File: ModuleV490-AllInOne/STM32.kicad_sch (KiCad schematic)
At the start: 45 parts, among them J10 RELAY, J11 TEMP1, J12 TEMP2, J13 TEMP3, J2 BOOT_MODE, J3 UART_PROG, J4 ST_LINK, J8 TXRX, Q1 AO3401A, U13 EL3H7(B)(TA)-G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

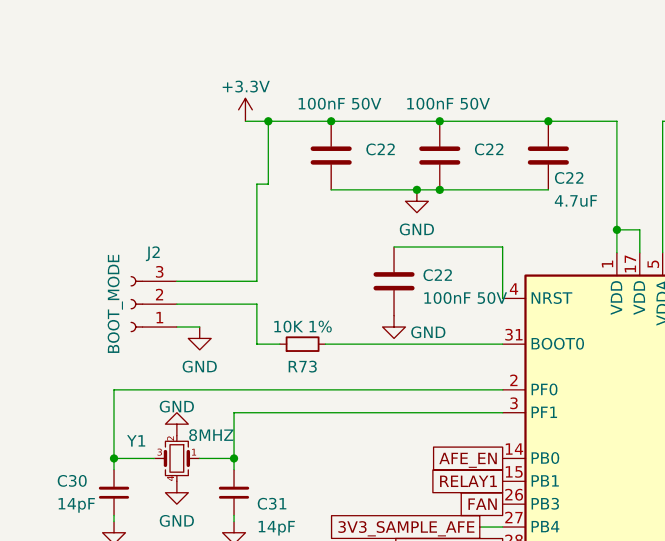
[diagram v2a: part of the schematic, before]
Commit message: Added SMT switch to replace jumper pins
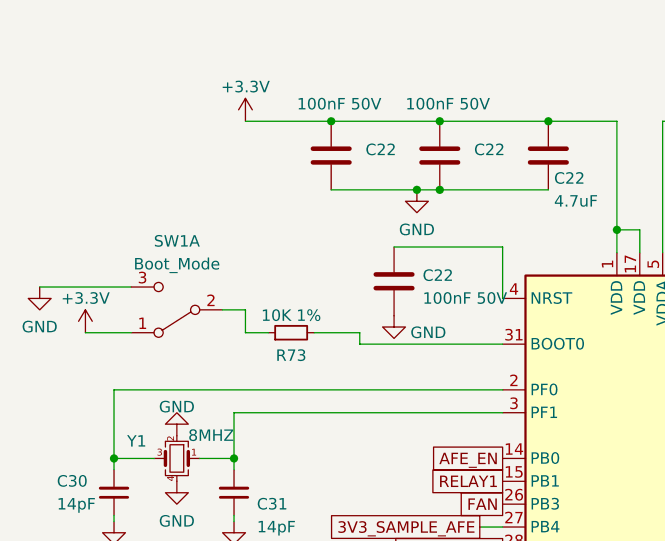
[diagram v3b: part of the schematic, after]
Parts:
- removed J2: BOOT_MODE, Connector_PinHeader_2.54mm:PinHeader_1x03_P2.54mm_Vertical, symbol Connector:Conn_01x03_Socket
- added SW1: Boot_Mode, SHOU_HAN:MST22D18G2 125, symbol Switch:SW_DPDT_x2
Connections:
- net +3.3V: now also SW1.1 (A)
- net GND: now also SW1.3 (C)
- net at R73.1: now also SW1.2 (B)
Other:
- moved on the sheet: R73
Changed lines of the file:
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@@
   (junction (at 214.63 138.43) (diameter 0) (color 0 0 0 0)
-  )
-  (junction (at 43.18 45.085) (diameter 0) (color 0 0 0 0)
   )
   (junction (at 39.37 82.55) (diameter 0) (color 0 0 0 0)
@@
   (no_connect (at 97.155 72.39))
   (no_connect (at 97.155 69.85))
+  (wire (pts (xy 53.34 68.58) (xy 53.34 69.85))
+    (stroke (width 0) (type default))
+  )
   (wire (pts (xy 93.345 52.705) (xy 95.885 52.705))
     (stroke (width 0) (type default))
@@
     (stroke (width 0) (type default))
   )
-  (wire (pts (xy 41.91 69.85) (xy 44.45 69.85))
+  (wire (pts (xy 40.64 68.58) (xy 43.18 68.58))
     (stroke (width 0) (type default))
   )
@@
     (stroke (width 0) (type default))
   )
-  (wire (pts (xy 49.53 69.85) (xy 69.215 69.85))
+  (wire (pts (xy 48.26 68.58) (xy 53.34 68.58))
     (stroke (width 0) (type default))
   )
@@
     (stroke (width 0) (type default))
   )
-  (wire (pts (xy 41.91 65.405) (xy 33.02 65.405))
-    (stroke (width 0) (type default))
-  )
   (wire (pts (xy 103.505 67.31) (xy 97.155 67.31))
     (stroke (width 0) (type default))
@@
     (stroke (width 0) (type default))
   )
+  (wire (pts (xy 40.64 68.58) (xy 40.64 66.04))
+    (stroke (width 0) (type default))
+  )
   (wire (pts (xy 97.155 92.71) (xy 139.065 92.71))
     (stroke (width 0) (type default))
@@
     (stroke (width 0) (type default))
   )
+  (wire (pts (xy 17.78 63.5) (xy 27.94 63.5))
+    (stroke (width 0) (type default))
+  )
   (wire (pts (xy 228.6 83.185) (xy 228.6 77.47))
     (stroke (width 0) (type default))
@@
     (stroke (width 0) (type default))
   )
-  (wire (pts (xy 41.91 69.85) (xy 41.91 65.405))
-    (stroke (width 0) (type default))
-  )
   (wire (pts (xy 55.88 176.53) (xy 55.88 177.8))
     (stroke (width 0) (type default))
@@
     (stroke (width 0) (type default))
   )
-  (wire (pts (xy 40.64 45.085) (xy 43.18 45.085))
-    (stroke (width 0) (type default))
-  )
-  (wire (pts (xy 33.02 67.945) (xy 35.56 67.945))
+  (wire (pts (xy 40.64 45.085) (xy 50.165 45.085))
     (stroke (width 0) (type default))
   )
@@
     (stroke (width 0) (type default))
   )
-  (wire (pts (xy 41.91 52.07) (xy 43.18 52.07))
-    (stroke (width 0) (type default))
-  )
   (wire (pts (xy 227.965 88.265) (xy 234.95 88.265))
     (stroke (width 0) (type default))
@@
     (stroke (width 0) (type default))
   )
-  (wire (pts (xy 43.18 52.07) (xy 43.18 45.085))
-    (stroke (width 0) (type default))
-  )
   (wire (pts (xy 84.455 59.69) (xy 84.455 57.15))
     (stroke (width 0) (type default))
@@
     (stroke (width 0) (type default))
   )
+  (wire (pts (xy 53.34 69.85) (xy 69.215 69.85))
+    (stroke (width 0) (type default))
+  )
   (wire (pts (xy 41.91 151.13) (xy 41.91 152.4))
     (stroke (width 0) (type default))
@@
     (stroke (width 0) (type default))
   )
+  (wire (pts (xy 22.86 68.58) (xy 27.94 68.58))
+    (stroke (width 0) (type default))
+  )
   (wire (pts (xy 26.035 88.9) (xy 26.035 89.535))
     (stroke (width 0) (type default))
   )
-  (wire (pts (xy 33.02 62.865) (xy 41.91 62.865))
-    (stroke (width 0) (type default))
-  )
   (wire (pts (xy 227.33 84.455) (xy 234.95 84.455))
     (stroke (width 0) (type default))
@@
     (stroke (width 0) (type default))
   )
-  (wire (pts (xy 43.18 45.085) (xy 50.165 45.085))
-    (stroke (width 0) (type default))
-  )
   (wire (pts (xy 194.31 137.795) (xy 194.31 134.62))
     (stroke (width 0) (type default))
   )
+  (wire (pts (xy 40.64 66.04) (xy 38.1 66.04))
+    (stroke (width 0) (type default))
+  )
   (wire (pts (xy 214.63 150.495) (xy 214.63 151.13))
     (stroke (width 0) (type default))
@@
   )
   (wire (pts (xy 103.505 64.77) (xy 97.155 64.77))
-    (stroke (width 0) (type default))
-  )
-  (wire (pts (xy 41.91 62.865) (xy 41.91 52.07))
     (stroke (width 0) (type default))
   )
@@
     )
   )
+  (symbol (lib_id "power:+3.3V") (at 22.86 68.58 0) (unit 1)
+    (in_bom yes) (on_board yes) (dnp no) (fields_autoplaced)
+    (property "Reference" "#PWR024" (at 22.86 72.39 0)
+      (effects (font (size 1.27 1.27)) hide)
+    )
+    (property "Value" "+3.3V" (at 22.86 64.77 0)
+      (effects (font (size 1.27 1.27)))
+    )
+    (property "Footprint" "" (at 22.86 68.58 0)
+      (effects (font (size 1.27 1.27)) hide)
+    )
+    (property "Datasheet" "" (at 22.86 68.58 0)
+      (effects (font (size 1.27 1.27)) hide)
+    )
+    (pin "1")
+    (instances
+      (project "Module_16S"
+        (path "/e63e39d7-6ac0-4ffd-8aa3-1841a4541b55"
+          (reference "#PWR024") (unit 1)
+        )
+        (path "/e63e39d7-6ac0-4ffd-8aa3-1841a4541b55/f65e9c34-bb90-4d0c-b988-67c6b9ba4d90"
+          (reference "#PWR08") (unit 1)
+        )
+      )
+    )
+  )
   (symbol (lib_id "Relay_SolidState:ASSR-1218") (at 45.72 179.07 0) (unit 1)
     (in_bom yes) (on_board yes) (dnp no) (fields_autoplaced)
@@
         (path "/e63e39d7-6ac0-4ffd-8aa3-1841a4541b55/f65e9c34-bb90-4d0c-b988-67c6b9ba4d90"
           (reference "TH3") (unit 1)
+        )
+      )
+    )
+  )
+  (symbol (lib_id "Switch:SW_DPDT_x2") (at 33.02 66.04 180) (unit 1)
+    (in_bom yes) (on_board yes) (dnp no) (fields_autoplaced)
+    (property "Reference" "SW1" (at 33.02 58.42 0)
+      (effects (font (size 1.27 1.27)))
+    )
+    (property "Value" "Boot_Mode" (at 33.02 60.96 0)
+      (effects (font (size 1.27 1.27)))
+    )
+    (property "Footprint" "SHOU_HAN:MST22D18G2 125" (at 33.02 66.04 0)
+      (effects (font (size 1.27 1.27)) hide)
+    )
+    (property "Datasheet" "~" (at 33.02 66.04 0)
+      (effects (font (size 1.27 1.27)) hide)
+    )
+    (property "LCSCStockCode" "C2906280" (at 33.02 66.04 0)
+      (effects (font (size 1.27 1.27)) hide)
+    )
+    (pin "1")
+    (pin "2")
+    (pin "3")
+    (pin "4")
+    (pin "5")
+    (pin "6")
+    (instances
+      (project "Module_16S"
+        (path "/e63e39d7-6ac0-4ffd-8aa3-1841a4541b55/f65e9c34-bb90-4d0c-b988-67c6b9ba4d90"
+          (reference "SW1") (unit 1)
         )
       )
@@
     )
   )
-  (symbol (lib_id "power:GND") (at 35.56 67.945 0) (unit 1)
-    (in_bom yes) (on_board yes) (dnp no) (fields_autoplaced)
-    (property "Reference" "#PWR036" (at 35.56 74.295 0)
-      (effects (font (size 1.27 1.27)) hide)
-    )
-    (property "Value" "GND" (at 35.56 72.39 0)
-      (effects (font (size 1.27 1.27)))
-    )
-    (property "Footprint" "" (at 35.56 67.945 0)
-      (effects (font (size 1.27 1.27)) hide)
-    )
-    (property "Datasheet" "" (at 35.56 67.945 0)
+  (symbol (lib_id "power:GND") (at 17.78 63.5 0) (unit 1)
+    (in_bom yes) (on_board yes) (dnp no) (fields_autoplaced)
+    (property "Reference" "#PWR036" (at 17.78 69.85 0)
+      (effects (font (size 1.27 1.27)) hide)
+    )
+    (property "Value" "GND" (at 17.78 67.945 0)
+      (effects (font (size 1.27 1.27)))
+    )
+    (property "Footprint" "" (at 17.78 63.5 0)
+      (effects (font (size 1.27 1.27)) hide)
+    )
+    (property "Datasheet" "" (at 17.78 63.5 0)
       (effects (font (size 1.27 1.27)) hide)
     )
@@
         (path "/e63e39d7-6ac0-4ffd-8aa3-1841a4541b55/f65e9c34-bb90-4d0c-b988-67c6b9ba4d90"
           (reference "D19") (unit 1)
-        )
-      )
-    )
-  )
-  (symbol (lib_id "Connector:Conn_01x03_Socket") (at 27.94 65.405 180) (unit 1)
-    (in_bom yes) (on_board yes) (dnp no)
-    (property "Reference" "J2" (at 30.48 59.69 0)
-      (effects (font (size 1.27 1.27)))
-    )
-    (property "Value" "BOOT_MODE" (at 26.035 65.405 90)
-      (effects (font (size 1.27 1.27)))
-    )
-    (property "Footprint" "Connector_PinHeader_2.54mm:PinHeader_1x03_P2.54mm_Vertical" (at 27.94 65.405 0)
-      (effects (font (size 1.27 1.27)) hide)
-    )
-    (property "Datasheet" "~" (at 27.94 65.405 0)
-      (effects (font (size 1.27 1.27)) hide)
-    )
-    (property "PartNumber" "DZ254R-11-03-63" (at 27.94 65.405 0)
-      (effects (font (size 1.27 1.27)) hide)
-    )
-    (property "LCSCStockCode" "C2935909" (at 27.94 65.405 0)
-      (effects (font (size 1.27 1.27)) hide)
-    )
-    (pin "1")
-    (pin "2")
-    (pin "3")
-    (instances
-      (project "Module_16S"
-        (path "/e63e39d7-6ac0-4ffd-8aa3-1841a4541b55/f65e9c34-bb90-4d0c-b988-67c6b9ba4d90"
-          (reference "J2") (unit 1)
         )
       )
@@
     )
   )
-  (symbol (lib_id "Device:R_Small") (at 46.99 69.85 90) (unit 1)
+  (symbol (lib_id "Device:R_Small") (at 45.72 68.58 90) (unit 1)
     (in_bom yes) (on_board yes) (dnp no)
-    (property "Reference" "R73" (at 46.99 72.39 90)
-      (effects (font (size 1.27 1.27)))
-    )
-    (property "Value" "10K 1%" (at 46.99 67.945 90)
-      (effects (font (size 1.27 1.27)))
-    )
-    (property "Footprint" "Resistor_SMD:R_0603_1608Metric" (at 46.99 69.85 0)
-      (effects (font (size 1.27 1.27)) hide)
-    )
-    (property "Datasheet" "~" (at 46.99 69.85 0)
-      (effects (font (size 1.27 1.27)) hide)
-    )
-    (property "PartNumber" "0603WAF1002T5E" (at 46.99 69.85 0)
-      (effects (font (size 1.27 1.27)) hide)
-    )
-    (property "LCSCStockCode" "C25804" (at 46.99 69.85 0)
-      (effects (font (size 1.27 1.27)) hide)
-    )
+    (property "Reference" "R73" (at 45.72 71.12 90)
+      (effects (font (size 1.27 1.27)))
+    )
+    (property "Value" "10K 1%" (at 45.72 66.675 90)
+      (effects (font (size 1.27 1.27)))
+    )
+    (property "Footprint" "Resistor_SMD:R_0603_1608Metric" (at 45.72 68.58 0)
+      (effects (font (size 1.27 1.27)) hide)
+    )
+    (property "Datasheet" "~" (at 45.72 68.58 0)
+      (effects (font (size 1.27 1.27)) hide)
+    )
+    (property "PartNumber" "0603WAF1002T5E" (at 45.72 68.58 0)
+      (effects (font (size 1.27 1.27)) hide)
+    )
+    (property "LCSCStockCode" "C25804" (at 45.72 68.58 0)
+      (effects (font (size 1.27 1.27)) hide)
+    )
